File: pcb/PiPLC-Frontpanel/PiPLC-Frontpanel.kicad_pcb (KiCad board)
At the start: 2 copper layers, 98 x 50 mm, 23 parts, among them J1 Conn_02x12_Odd_Even, J2 KNX

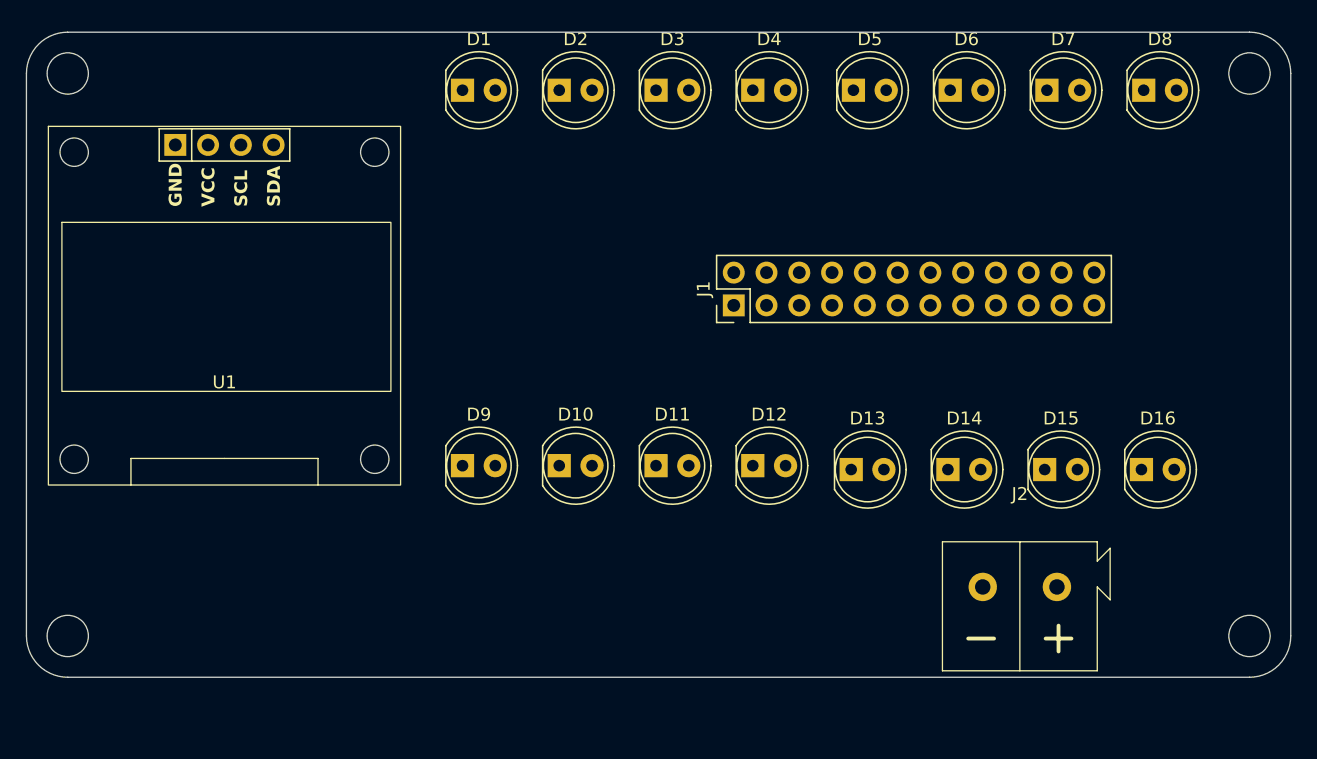
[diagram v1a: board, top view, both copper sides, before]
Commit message: [HMI] Move mechanical bits
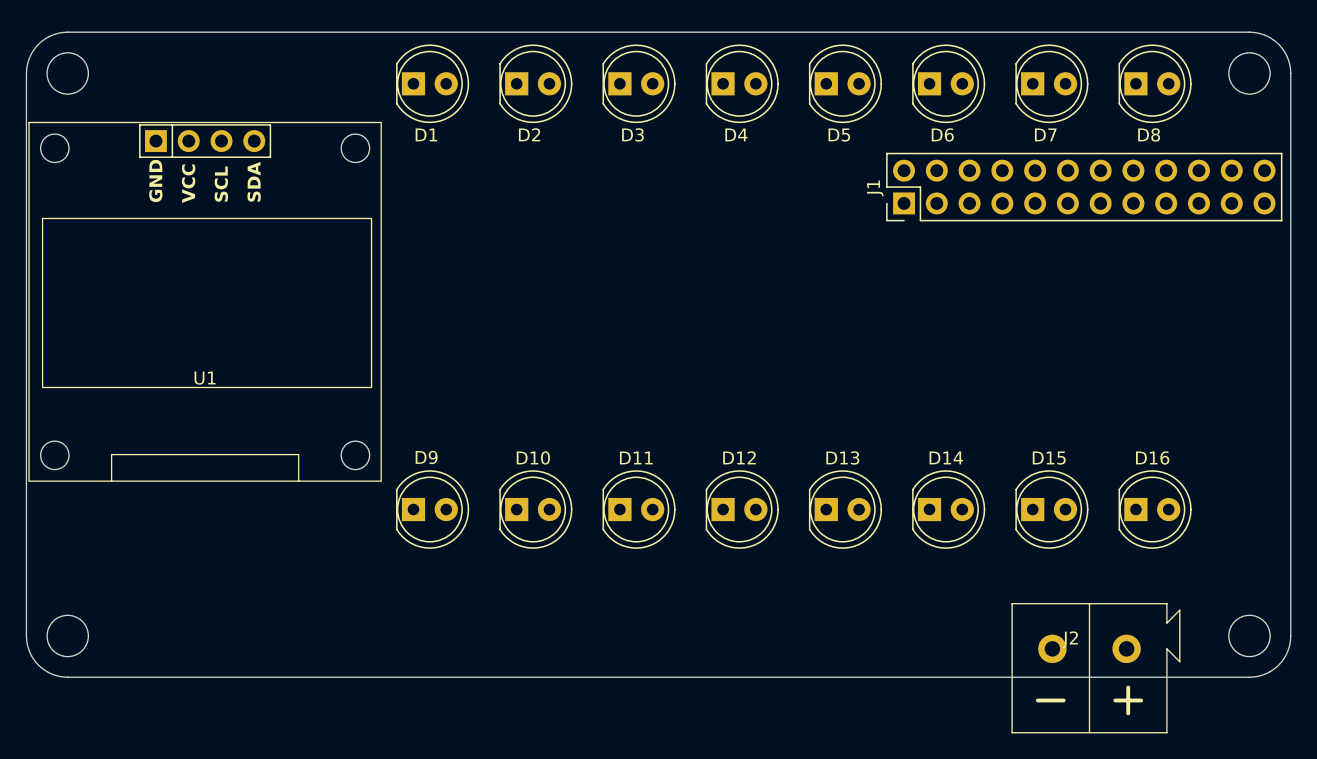
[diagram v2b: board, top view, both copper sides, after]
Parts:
- moved J1 15.4 mm to (185.9, 80.1)
- moved J2 7.22 mm to (200.3, 114.6)
- moved D9 5.10 mm to (147.9, 103.8)
- moved D10 4.74 mm to (155.9, 103.8)
- moved D11 4.40 mm to (163.9, 103.8)
- moved D12 4.10 mm to (171.9, 103.8)
- moved D1 3.83 mm to (147.9, 70.8)
- moved D13 3.65 mm to (179.9, 103.8)
- moved D14 3.41 mm to (187.9, 103.8)
- moved D2 3.34 mm to (155.9, 70.8)
- moved D15 3.24 mm to (195.9, 103.8)
- moved D16 3.13 mm to (203.9, 103.8)
- moved D3 2.84 mm to (163.9, 70.8)
- moved D4 2.35 mm to (171.9, 70.8)
- moved D5 2.16 mm to (179.9, 70.8)
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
